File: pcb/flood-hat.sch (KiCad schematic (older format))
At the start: 20 parts, among them J1 PI2GPIO, P1 CONN_01X04, P2 CONN_01X04, P3 CONN_01X02, P4 CONN_01X02, Q1 AO3401, U1 CAT24C32, U2 DMMT5401

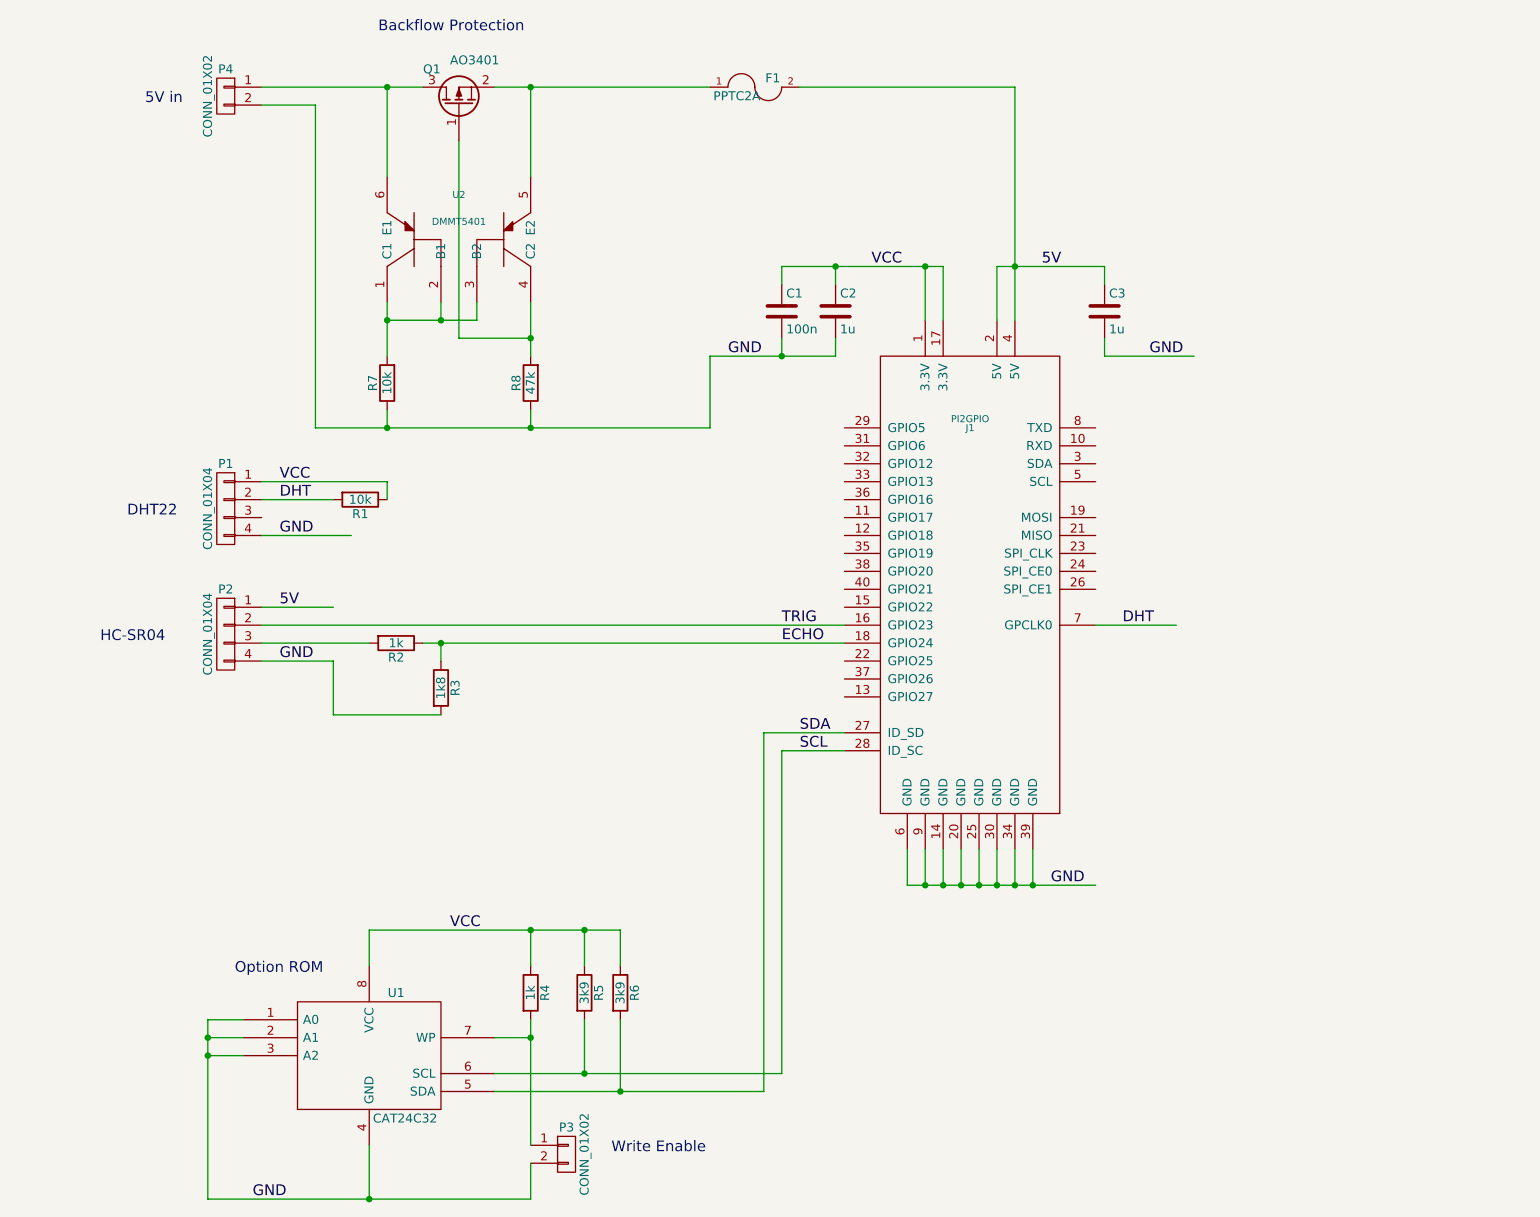
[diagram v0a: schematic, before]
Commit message: modified schematic to include STM32 for power control.
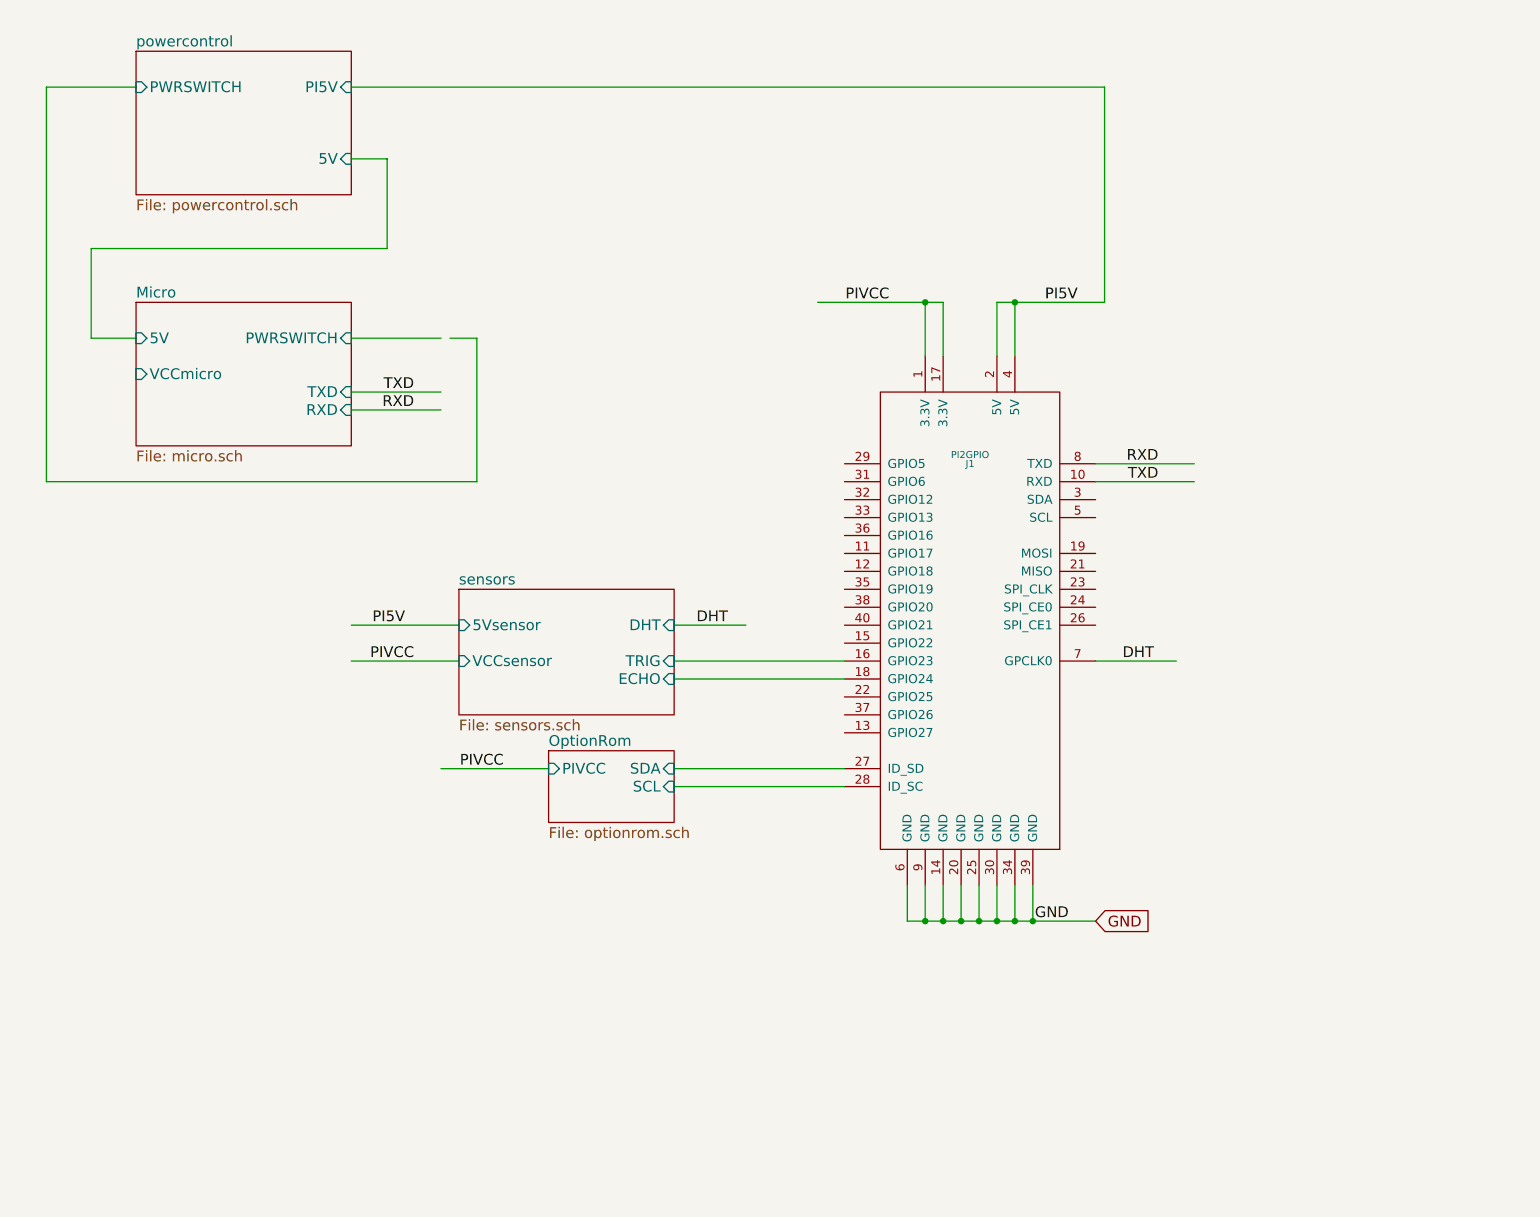
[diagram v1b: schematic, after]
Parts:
- removed C1: 100n, Capacitors_SMD:C_0805, symbol C
- removed C2, C3: 1u, Capacitors_SMD:C_0805, symbol C
- removed F1: PPTC2A, Resistors_SMD:R_1812, symbol FUSE
- removed P1, P2: CONN_01X04, Pin_Headers:Pin_Header_Angled_1x04, symbol CONN_01X04
- removed P3: CONN_01X02, Pin_Headers:Pin_Header_Straight_1x02, symbol CONN_01X02
- removed P4: CONN_01X02, Terminal_Blocks:TerminalBlock_Pheonix_MKDS1.5-2pol, symbol CONN_01X02
- removed Q1: AO3401, TO_SOT_Packages_SMD:SOT-23, symbol Q_PMOS_GSD
- removed R1, R7: 10k, Resistors_SMD:R_0805, symbol R
- removed R2, R4: 1k, Resistors_SMD:R_0805, symbol R
- removed R3: 1k8, Resistors_SMD:R_0805, symbol R
- removed R5, R6: 3k9, Resistors_SMD:R_0805, symbol R
- removed R8: 47k, Resistors_SMD:R_0805, symbol R
- removed U1: CAT24C32, SMD_Packages:SOIC-8-N, symbol 24C16
- removed U2: DMMT5401, TO_SOT_Packages_SMD:TSOT-6-MK06A, symbol PNP2
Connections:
- net labels added: PI5V, PIVCC, RXD, TXD
- net labels removed: 5V, ECHO, SCL, SDA, TRIG, VCC
- wire segments 76 -> 41
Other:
- note removed: "5V in"
- note removed: "Backflow Protection"
- note removed: "DHT22"
- note removed: "HC-SR04"
- note removed: "Option ROM"
- note removed: "Write Enable"
- moved on the sheet: J1

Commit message: allow STM32 to control option-ROM WP pin.
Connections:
- net labels added: ECHO, SWITCH, TRIG, WP
- wire segments 41 -> 39
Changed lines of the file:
@@
 F3 "SDA" I R 5800 4900 60
 F4 "PIVCC" I L 5100 4900 60
+F5 "WP" I L 5100 5100 60
 $EndSheet
 Wire Wire Line
@@
 F5 "RXD" I R 4000 2900 60
 F6 "VCCmicro" I L 2800 2700 60
+F7 "WP" I R 4000 3000 60
 $EndSheet
 Wire Wire Line
-	4000 2500 4500 2500
+	4000 2500 4700 2500
 Wire Wire Line
 	4000 1500 4200 1500
@@
 	8200 1100 8200 2300
 Wire Wire Line
-	4550 2500 4700 2500
-Wire Wire Line
-	4700 2500 4700 3300
-Wire Wire Line
-	4700 3300 2300 3300
-Wire Wire Line
-	2300 3300 2300 1100
-Wire Wire Line
 	2300 1100 2800 1100
 Wire Wire Line
@@
 Text Label 4850 4900 2    60   ~ 0
 PIVCC
+Wire Wire Line
+	5100 5100 4500 5100
+Text Label 4850 5100 2    60   ~ 0
+WP
+Wire Wire Line
+	4000 3000 4500 3000
+Text Label 4350 3000 2    60   ~ 0
+WP
+Text Label 4550 2500 2    60   ~ 0
+SWITCH
+Text Label 2700 1100 2    60   ~ 0
+SWITCH
+Text Label 6500 4300 2    60   ~ 0
+TRIG
+Text Label 6500 4400 2    60   ~ 0
+ECHO
 $EndSCHEMATC

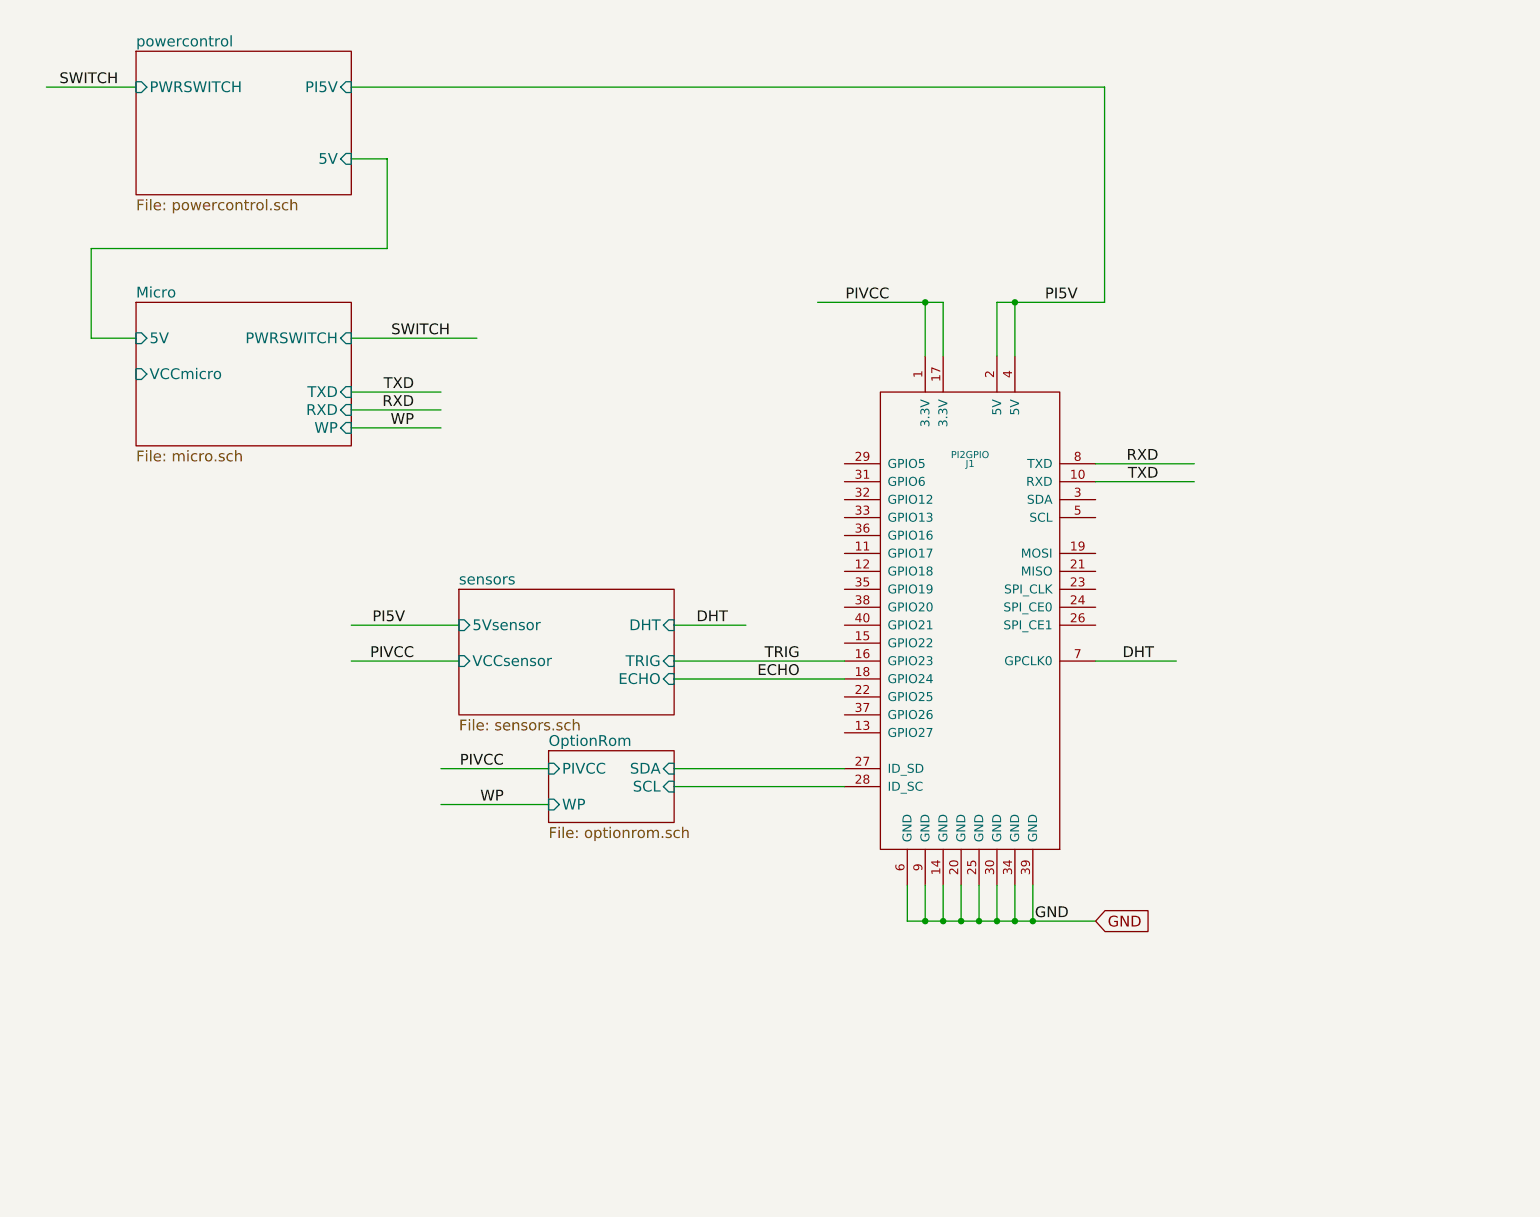
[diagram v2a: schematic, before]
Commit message: added SPI flash and connections for STM32 to control the sensors
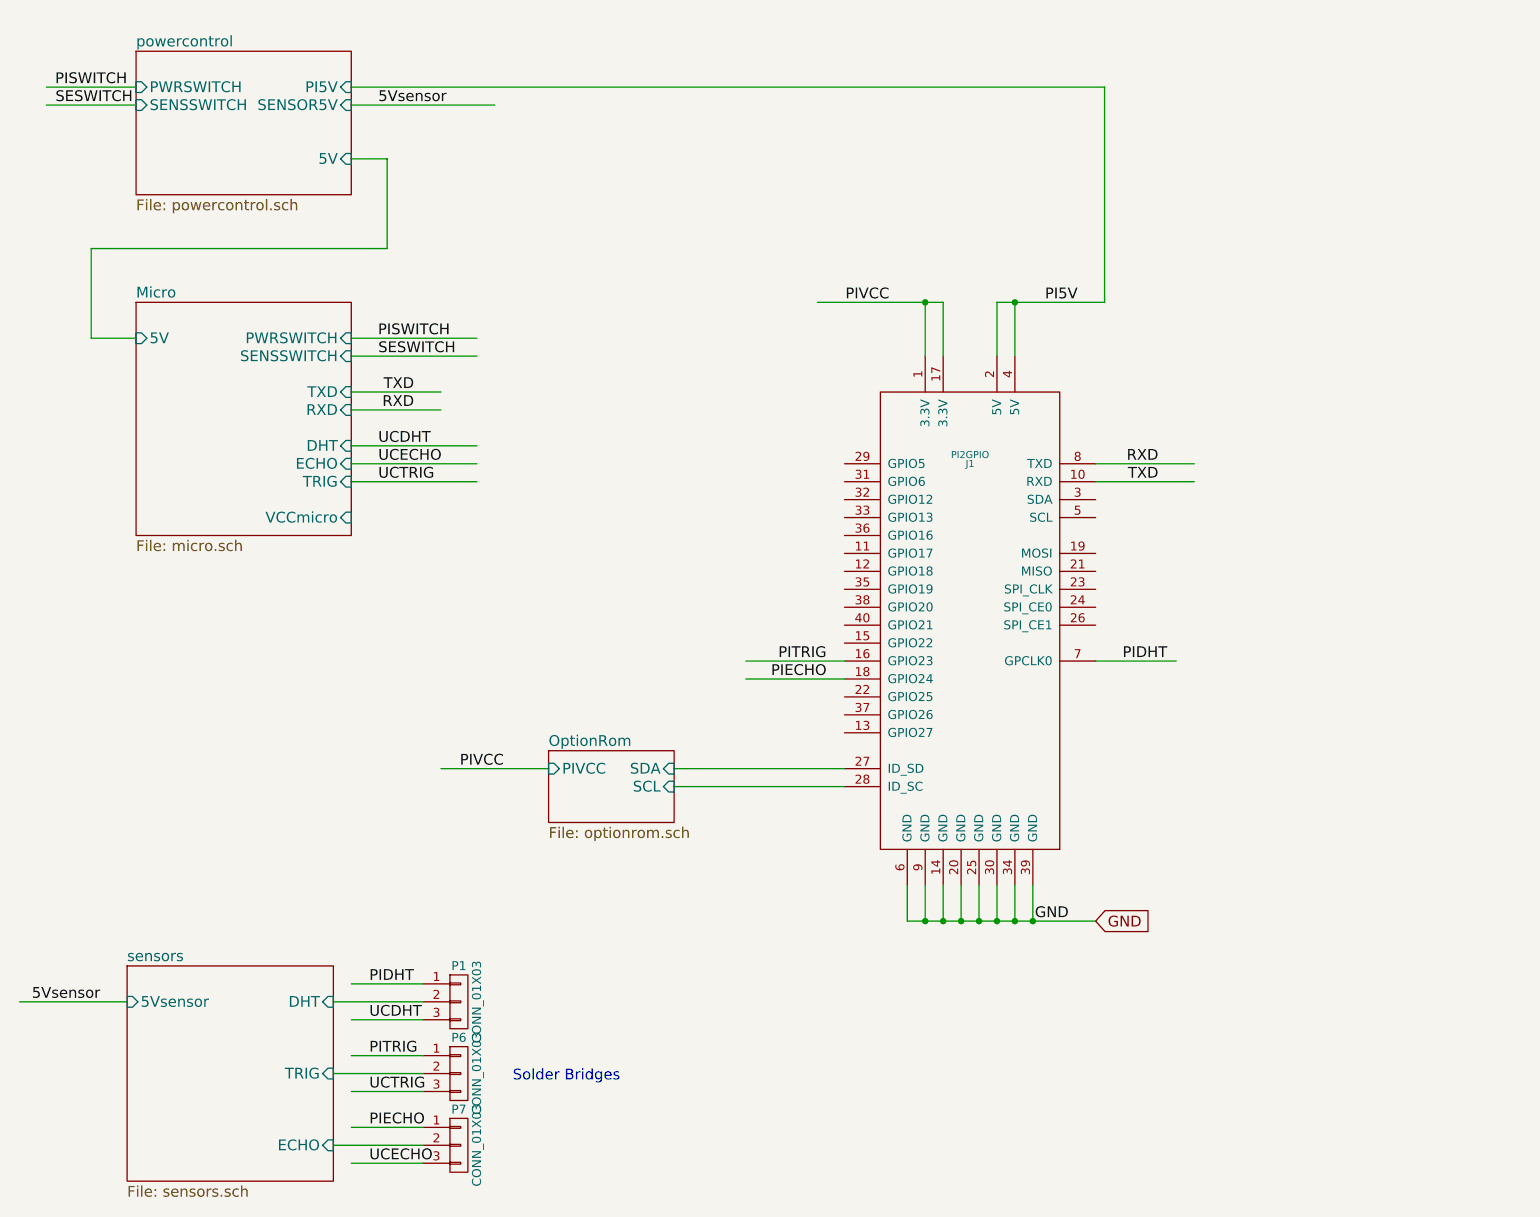
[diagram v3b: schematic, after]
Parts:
- added P1, P6, P7: CONN_01X03, smd:SMD_solder_bridge_3pin, symbol CONN_01X03
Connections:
- net labels added: 5Vsensor, PIDHT, PIECHO, PISWITCH, PITRIG, SESWITCH, UCDHT, UCECHO, UCTRIG
- net labels removed: DHT, ECHO, SWITCH, TRIG, WP
- wire segments 39 -> 50
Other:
- note added: "Solder Bridges"
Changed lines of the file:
@@
 $EndComp
 Text Label 8300 4300 0    60   ~ 0
-DHT
+PIDHT
 $Sheet
 S 5100 4800 700  400
@@
 F3 "SDA" I R 5800 4900 60
 F4 "PIVCC" I L 5100 4900 60
-F5 "WP" I L 5100 5100 60
 $EndSheet
 Wire Wire Line
@@
 F3 "PI5V" I R 4000 1100 60
 F4 "5V" I R 4000 1500 60
+F5 "SENSSWITCH" I L 2800 1200 60
+F6 "SENSOR5V" I R 4000 1200 60
 $EndSheet
 Text GLabel 8150 5750 2    60   Input ~ 0
@@
 	7700 2300 7700 2600
 $Sheet
-S 4600 3900 1200 700
+S 2750 6000 1150 1200
 U 57B33DBD
 F0 "sensors" 60
 F1 "sensors.sch" 60
-F2 "TRIG" I R 5800 4300 60
-F3 "ECHO" I R 5800 4400 60
-F4 "DHT" I R 5800 4100 60
-F5 "5Vsensor" I L 4600 4100 60
-F6 "VCCsensor" I L 4600 4300 60
-$EndSheet
-Wire Wire Line
-	6750 4300 5800 4300
-Wire Wire Line
-	5800 4400 6750 4400
-Wire Wire Line
-	5800 4100 6200 4100
-Text Label 6100 4100 2    60   ~ 0
-DHT
+F2 "TRIG" I R 3900 6600 60
+F3 "ECHO" I R 3900 7000 60
+F4 "DHT" I R 3900 6200 60
+F5 "5Vsensor" I L 2750 6200 60
+$EndSheet
+Wire Wire Line
+	3900 6200 4400 6200
 Wire Wire Line
 	7600 2300 8200 2300
 $Sheet
-S 2800 2300 1200 800
+S 2800 2300 1200 1300
 U 57B35E6C
 F0 "Micro" 60
@@
 F4 "TXD" I R 4000 2800 60
 F5 "RXD" I R 4000 2900 60
-F6 "VCCmicro" I L 2800 2700 60
-F7 "WP" I R 4000 3000 60
+F6 "VCCmicro" I R 4000 3500 60
+F7 "DHT" I R 4000 3100 60
+F8 "ECHO" I R 4000 3200 60
+F9 "TRIG" I R 4000 3300 60
+F10 "SENSSWITCH" I R 4000 2600 60
 $EndSheet
 Wire Wire Line
@@
 	2300 1100 2800 1100
 Wire Wire Line
-	4000 4300 4600 4300
-Wire Wire Line
-	4600 4100 4000 4100
-Text Label 4300 4100 2    60   ~ 0
-PI5V
+	2750 6200 2150 6200
+Text Label 2600 6200 2    60   ~ 0
+5Vsensor
 Text Label 7000 2300 2    60   ~ 0
 PIVCC
 Wire Wire Line
 	5100 4900 4500 4900
-Text Label 4350 4300 2    60   ~ 0
-PIVCC
 Text Label 4850 4900 2    60   ~ 0
 PIVCC
-Wire Wire Line
-	5100 5100 4500 5100
-Text Label 4850 5100 2    60   ~ 0
-WP
-Wire Wire Line
-	4000 3000 4500 3000
-Text Label 4350 3000 2    60   ~ 0
-WP
 Text Label 4550 2500 2    60   ~ 0
-SWITCH
-Text Label 2700 1100 2    60   ~ 0
-SWITCH
-Text Label 6500 4300 2    60   ~ 0
-TRIG
-Text Label 6500 4400 2    60   ~ 0
-ECHO
+PISWITCH
+Text Label 2750 1100 2    60   ~ 0
+PISWITCH
+Text Label 6650 4300 2    60   ~ 0
+PITRIG
+Text Label 6650 4400 2    60   ~ 0
+PIECHO
+Wire Wire Line
+	4000 2600 4700 2600
+Text Label 4150 2600 0    60   ~ 0
+SESWITCH
+Wire Wire Line
+	2800 1200 2300 1200
+Text Label 2350 1200 0    60   ~ 0
+SESWITCH
+Wire Wire Line
+	6200 4300 6750 4300
+Wire Wire Line
+	6750 4400 6200 4400
+$Comp
+L CONN_01X03 P1
+U 1 1 57B619C9
+P 4600 6200
+F 0 "P1" H 4600 6400 50  0000 C CNN
+F 1 "CONN_01X03" V 4700 6200 50  0000 C CNN
+F 2 "smd:SMD_solder_bridge_3pin" H 4600 6200 50  0001 C CNN
+F 3 "" H 4600 6200 50  0000 C CNN
+	1    4600 6200
+	1    0    0    -1
+$EndComp
+$Comp
+L CONN_01X03 P6
+U 1 1 57B62C59
+P 4600 6600
+F 0 "P6" H 4600 6800 50  0000 C CNN
+F 1 "CONN_01X03" V 4700 6600 50  0000 C CNN
+F 2 "smd:SMD_solder_bridge_3pin" H 4600 6600 50  0001 C CNN
+F 3 "" H 4600 6600 50  0000 C CNN
+	1    4600 6600
+	1    0    0    -1
+$EndComp
+$Comp
+L CONN_01X03 P7
+U 1 1 57B62DBD
+P 4600 7000
+F 0 "P7" H 4600 7200 50  0000 C CNN
+F 1 "CONN_01X03" V 4700 7000 50  0000 C CNN
+F 2 "smd:SMD_solder_bridge_3pin" H 4600 7000 50  0001 C CNN
+F 3 "" H 4600 7000 50  0000 C CNN
+	1    4600 7000
+	1    0    0    -1
+$EndComp
+Wire Wire Line
+	4400 6100 4000 6100
+Wire Wire Line
+	4400 6300 4000 6300
+Wire Wire Line
+	3900 6600 4400 6600
+Wire Wire Line
+	3900 7000 4400 7000
+Wire Wire Line
+	4000 6500 4400 6500
+Wire Wire Line
+	4000 6700 4400 6700
+Wire Wire Line
+	4000 6900 4400 6900
+Wire Wire Line
+	4000 7100 4400 7100
+Wire Wire Line
+	4000 3100 4700 3100
+Wire Wire Line
+	4700 3200 4000 3200
+Wire Wire Line
+	4700 3300 4000 3300
+Text Label 4150 3100 0    60   ~ 0
+UCDHT
+Text Label 4150 3200 0    60   ~ 0
+UCECHO
+Text Label 4150 3300 0    60   ~ 0
+UCTRIG
+Text Label 4100 6100 0    60   ~ 0
+PIDHT
+Text Label 4100 6300 0    60   ~ 0
+UCDHT
+Text Label 4100 6500 0    60   ~ 0
+PITRIG
+Text Label 4100 6700 0    60   ~ 0
+UCTRIG
+Text Label 4100 6900 0    60   ~ 0
+PIECHO
+Text Label 4100 7100 0    60   ~ 0
+UCECHO
+Wire Wire Line
+	4000 1200 4800 1200
+Text Label 4150 1200 0    60   ~ 0
+5Vsensor
+Text Notes 4900 6650 0    60   ~ 0
+Solder Bridges
 $EndSCHEMATC
